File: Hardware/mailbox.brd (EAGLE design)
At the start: 36.8 x 36.8 mm, 24 parts, among them U3 V_REG_LDOSMD, U5 MCP73831

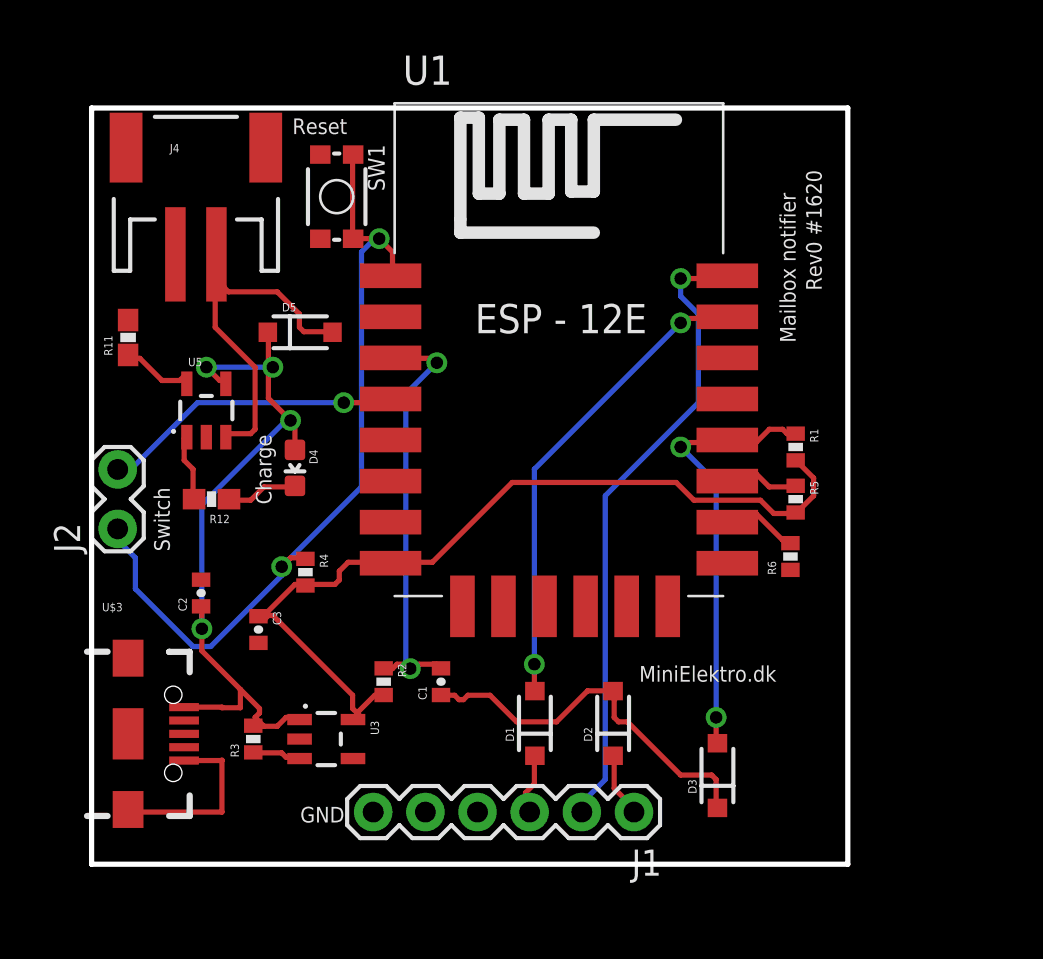
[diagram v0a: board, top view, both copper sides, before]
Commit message: Added battery measure + PDF schematic
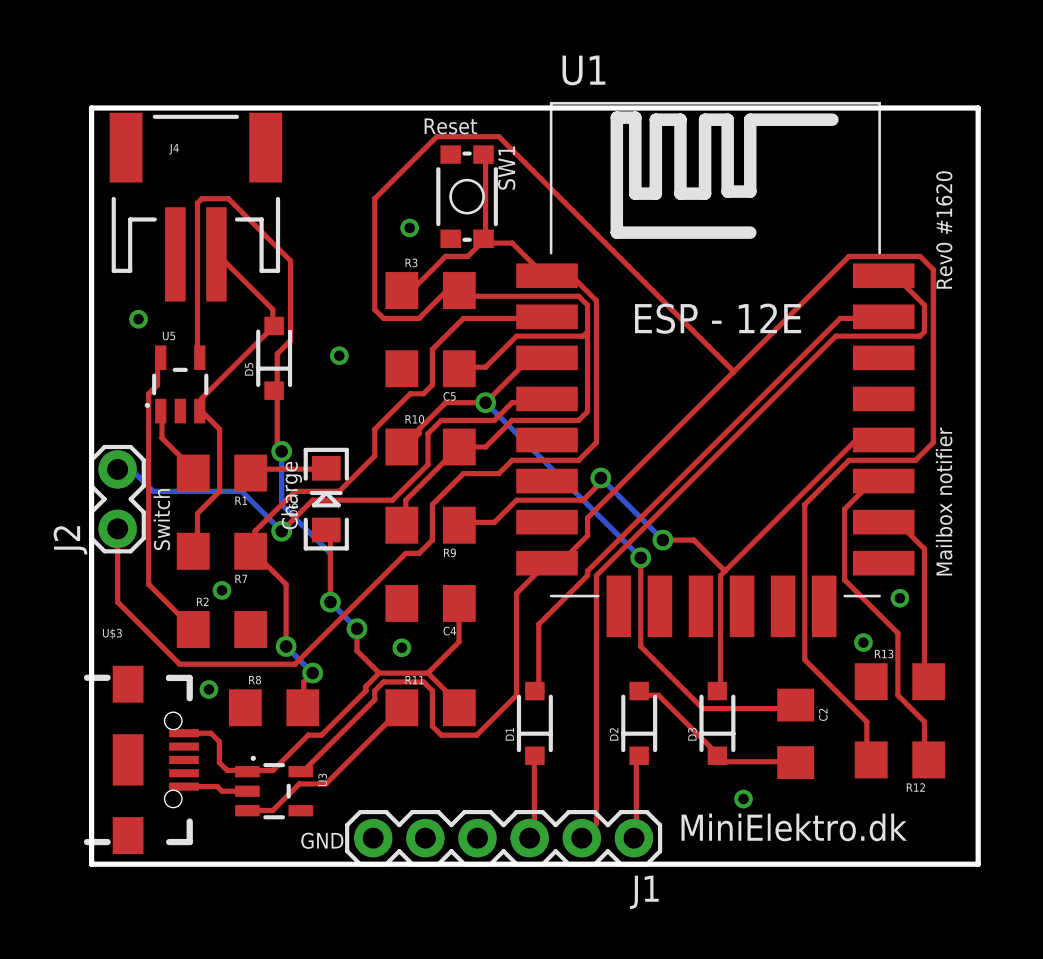
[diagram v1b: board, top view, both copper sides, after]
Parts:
- removed C1: 100nF, SparkFun-Passives:0402-CAP
- removed C3: 10uF, SparkFun-Passives:0402-CAP
- removed D4: Yellow, SparkFun-LED:LED-0603
- removed R4, R5, R6: 10K, SparkFun-Passives:0402-RES
- added C4, C5: 10uF, SparkFun-Passives:1206
- added D6: YELLOW, SparkFun-LED:LED-1206
- added R10, R13, R9: 10K, SparkFun-Passives:1206
- added R7: 1M, SparkFun-Passives:1206
- added R8: 220, SparkFun-Passives:1206
- C2: value 10uF -> 100nF; device SparkFun-Passives:0402-CAP -> SparkFun-Passives:1206
- R1: value 10K -> 1K; device SparkFun-Passives:0402-RES -> SparkFun-Passives:1206
- R11: value 2K -> 10K; device SparkFun-Passives:0603-RES -> SparkFun-Passives:1206
- R12: value 1K -> 10K; device SparkFun-Passives:0603-RES -> SparkFun-Passives:1206
- R2: value 10K -> 2K; device SparkFun-Passives:0402-RES -> SparkFun-Passives:1206
- R3: device SparkFun-Passives:0402-RES -> SparkFun-Passives:1206
- moved R12 35.9 mm to (38.1, 6.35)
- moved C2 29.8 mm to (33.0, 7.62), turned to 270 degrees
- moved R1 28.0 mm to (5.08, 20.3), turned to 180 degrees
- moved R3 23.5 mm to (15.2, 29.2), turned to 0 degrees
- moved R11 23.3 mm to (15.2, 8.89), turned to 0 degrees
- moved R2 8.27 mm to (5.08, 12.7), turned to 0 degrees
- moved U1 7.62 mm to (29.2, 24.1)
- moved SW1 6.35 mm to (17.0, 33.8)
- moved U3 3.59 mm to (7.62, 4.83)
- moved D3 2.54 mm to (29.2, 8.13)
- moved U5 1.80 mm to (3.05, 24.6)
- moved D5 1.80 mm to (7.62, 25.9), turned to 90 degrees
- moved U$3 1.27 mm to (0.51, 6.35)
- moved J1 1.27 mm to (25.1, 2.54)
- moved D2 1.27 mm to (25.4, 8.13)
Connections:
- net 3.3V: now also C5.1, R10.2, R12.2, R3.2, R9.2; no longer C3.1, R1.2, R2.2, R4.2, R5.2
- net ADC: now also R7.1, R8.2
- net CH_PD: now also C2.1, R10.1; no longer C1.2, R2.1
- net GND: now also C4.2, C5.2, R13.1, R2.2, R8.1; no longer C2.2, C3.2, R11.2, R6.1
- net GPIO0: now also R9.1; no longer R1.1
- net GPIO15: now also R13.2; no longer R6.2
- net GPIO2: now also R12.1; no longer R5.1
- net LDO_EN: now also R11.1; no longer R3.1
- net N$1: now also D6.C, R1.1; no longer D4.C, R12.1
- net N$3: now also C2.2; no longer C1.1
- net N$6: now also R1.2; no longer R12.2
- net N$7: now also R2.1; no longer R11.1
- net RESET: now also R3.1; no longer R4.1
- net V_BATT: now also R7.2
- net V_USB: now also C4.1, D6.A, R11.2; no longer C2.1, D4.A, R3.2
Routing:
- net 3.3V: track 43.1 -> 142.4 mm
- net ADC: track 0.00 -> 30.5 mm, vias 0 -> 2
- net V_USB: track 36.6 -> 61.4 mm, vias 4 -> 3
- net RESET: track 40.4 -> 56.6 mm, vias 2 -> 0
- net GPIO2: track 3.77 -> 16.4 mm
- net CH_PD: track 21.2 -> 32.8 mm
- net GPIO16: track 14.7 -> 25.8 mm
- net GPIO0: track 21.3 -> 32.3 mm
- net N$7: track 3.83 -> 14.4 mm
- net N$3: track 19.1 -> 9.13 mm
- net LDO_EN: track 2.40 -> 9.60 mm
- net TXD: track 31.0 -> 37.9 mm, vias 1 -> 0
- net GND: track 9.08 -> 3.18 mm, vias 0 -> 9
- net GPIO15: track 3.89 -> 9.07 mm
- net RXD: track 23.3 -> 26.5 mm, vias 2 -> 0
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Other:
- board size 36.8 x 36.8 mm -> 43.2 x 36.8 mm
